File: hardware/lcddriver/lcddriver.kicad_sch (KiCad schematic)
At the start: 28 parts, among them J1 Header, J2 UPDI, J3 I2C, SW1 C&K PTS526, SW2 C&K PTS526, U1 AVR32DB48, U2 LCD-S401C52TR, Y1 32.768kHz 12.5pF

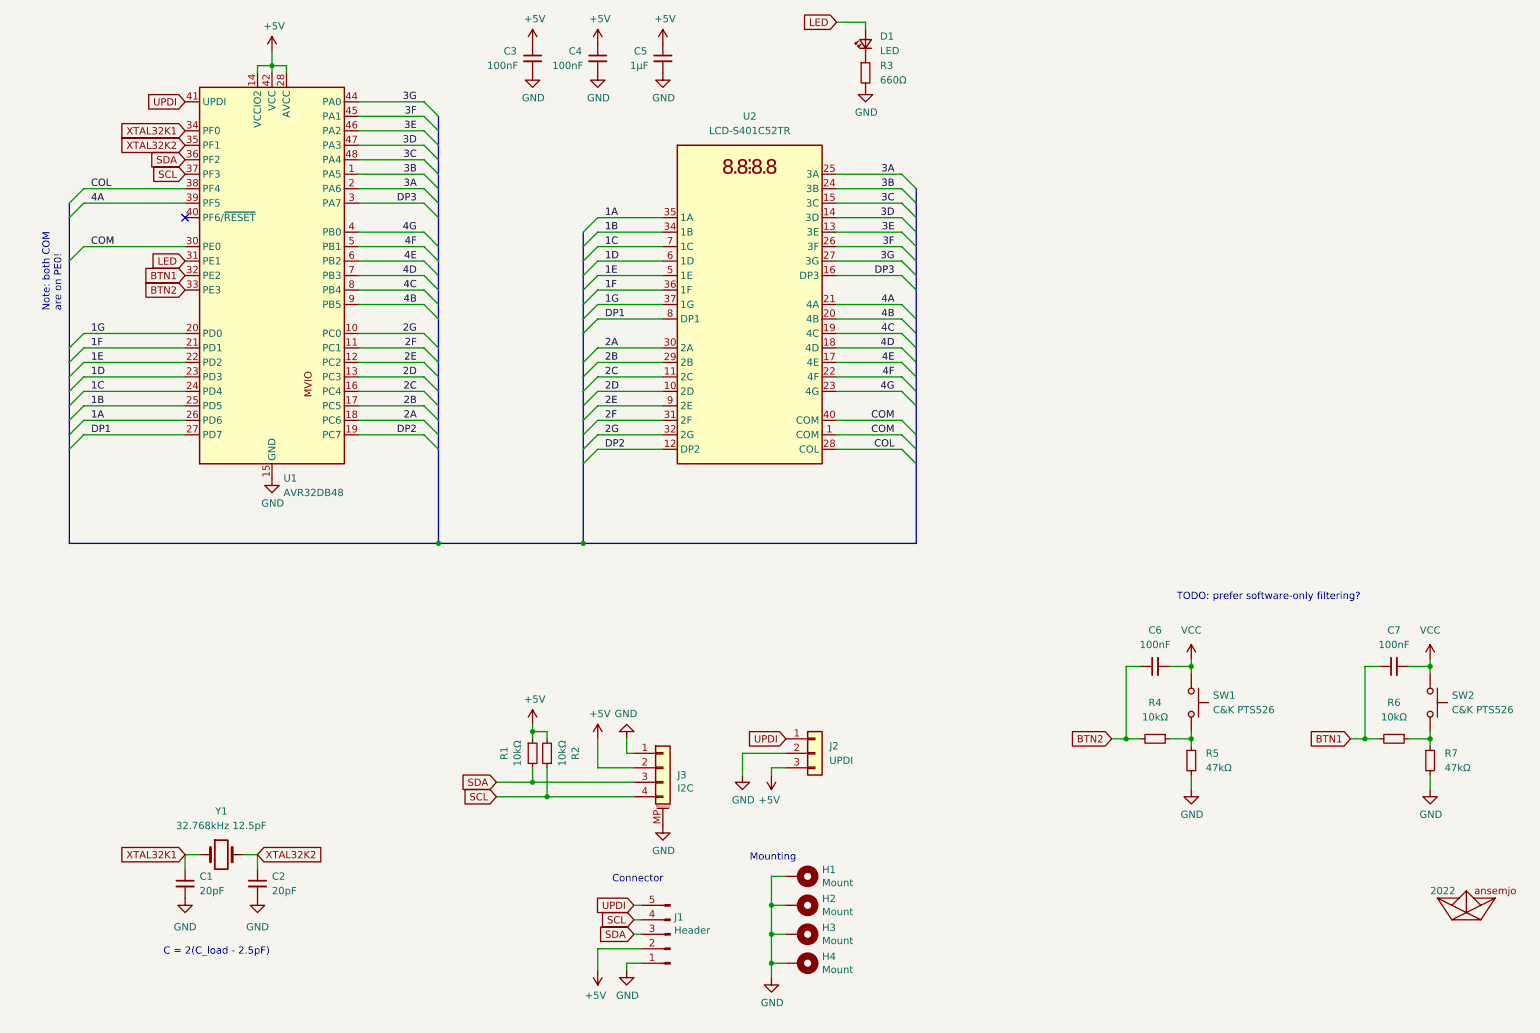
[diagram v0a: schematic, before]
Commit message: hw: finished routing lcd clock face
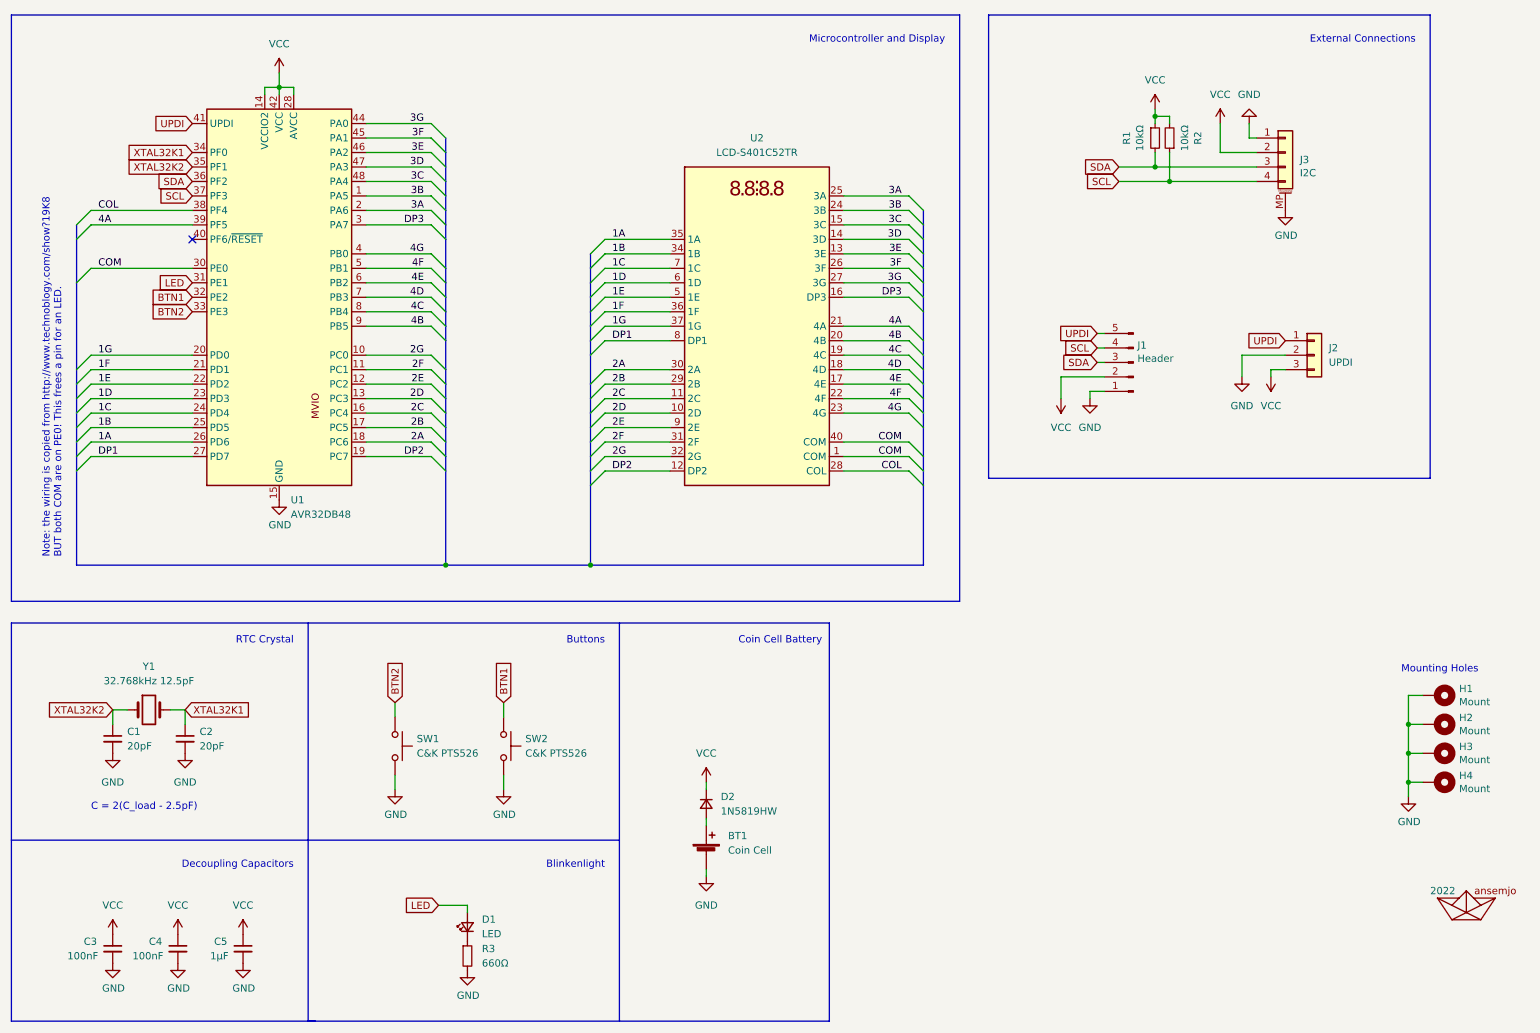
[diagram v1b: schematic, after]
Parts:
- removed C6, C7: 100nF, Capacitor_SMD:C_0805_2012Metric_Pad1.18x1.45mm_HandSolder, symbol Device:C_Small
- removed R4, R6: 10kΩ, Resistor_SMD:R_0805_2012Metric_Pad1.20x1.40mm_HandSolder, symbol Device:R_Small
- removed R5, R7: 47kΩ, Resistor_SMD:R_0805_2012Metric_Pad1.20x1.40mm_HandSolder, symbol Device:R_Small
- added BT1: Coin Cell, Battery:BatteryHolder_Keystone_3034_1x20mm, symbol Device:Battery_Cell
- added D2: 1N5819HW, Diode_SMD:D_SOD-123, symbol Device:D_Small
- A1: footprint ansemjo:ahoi-mask -> ansemjo:ahoi
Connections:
- net +5V is gone; now on net VCC: C3.1, C4.1, C5.1, J1.2 (Pin_2), J2.3 (Pin_3), J3.2 (Pin_2), R1.1, R2.2, U1.14 (VCCIO2), U1.28 (AVCC), U1.42 (VCC)
- net BTN1: now also SW2.1
- net BTN2: now also SW1.1
- net GND: now also SW1.2, SW2.2, BT1.2 (-)
- net VCC: now also D2.1 (K); no longer SW1.1, SW2.1
- net XTAL32K1: now also C2.1, Y1.2; no longer C1.1, Y1.1
- net XTAL32K2: now also C1.1, Y1.1; no longer C2.1, Y1.2
- new net: BT1.1 (+), D2.2 (A)
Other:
- note added: "Blinkenlight"
- note added: "Buttons"
- note added: "Coin Cell Battery"
- note added: "Decoupling Capacitors"
- note added: "External Connections"
- note added: "Microcontroller and Display"
- note added: "Mounting Holes"
- note added: "Note: the wiring is copied from http://www.technoblogy.com/show?19K8 BUT both COM are on PE0! This frees a pin for an LED."
- note added: "RTC Crystal"
- note removed: "Connector"
- note removed: "Mounting"
- note removed: "Note: both COM are on PE0!"
- note removed: "TODO: prefer software-only filtering?"
- title: VFD Driver Board -> LCD Driver Board
- moved on the sheet: C1, C2, C3, C4, C5, D1, H1, H2, H3, H4, J1, J2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
